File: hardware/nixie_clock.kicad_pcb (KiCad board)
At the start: 2 copper layers, 224 x 70 mm, 66 parts, among them J1 Conn_02x02_Odd_Even, J2 USB_C_Receptacle_USB2.0_16P, J3 Conn_01x03, Q1 IRF740, SW1 SW_SPST, SW2 SW_SPST, U1 AP63203WU, U2 MAX1771xSA, U3 ESP32-C3-WROOM-02, U4 HV5622PG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

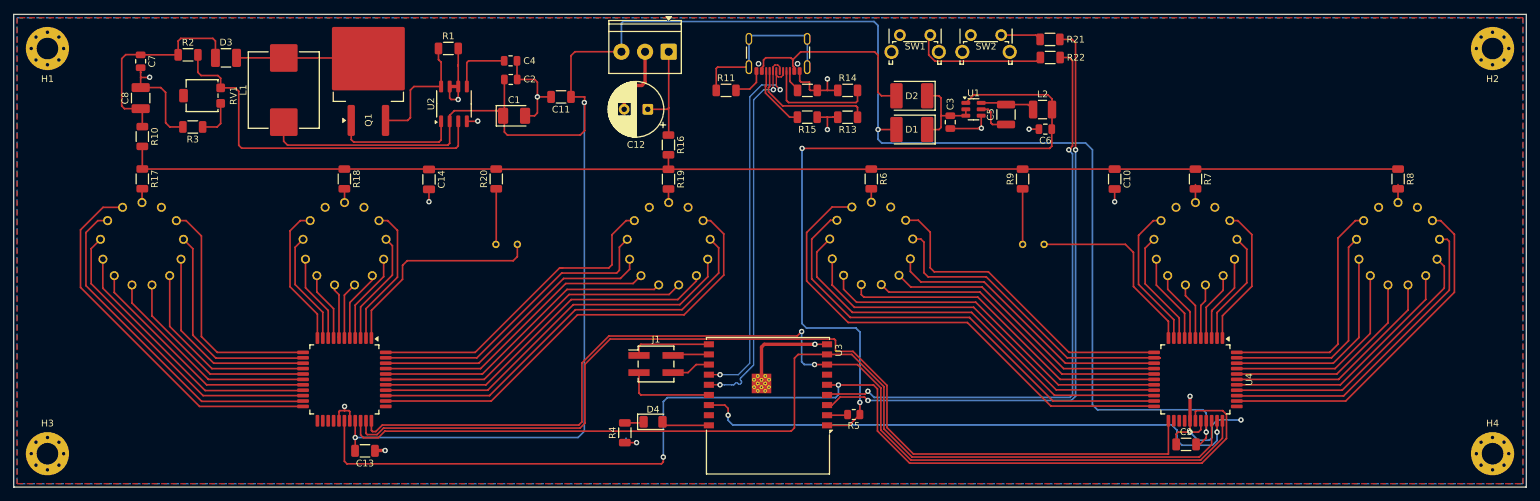
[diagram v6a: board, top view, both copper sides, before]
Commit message: Add decoupling capacitor for MCU. Fix circuit to avoid VCC being between capacitor and power pad.
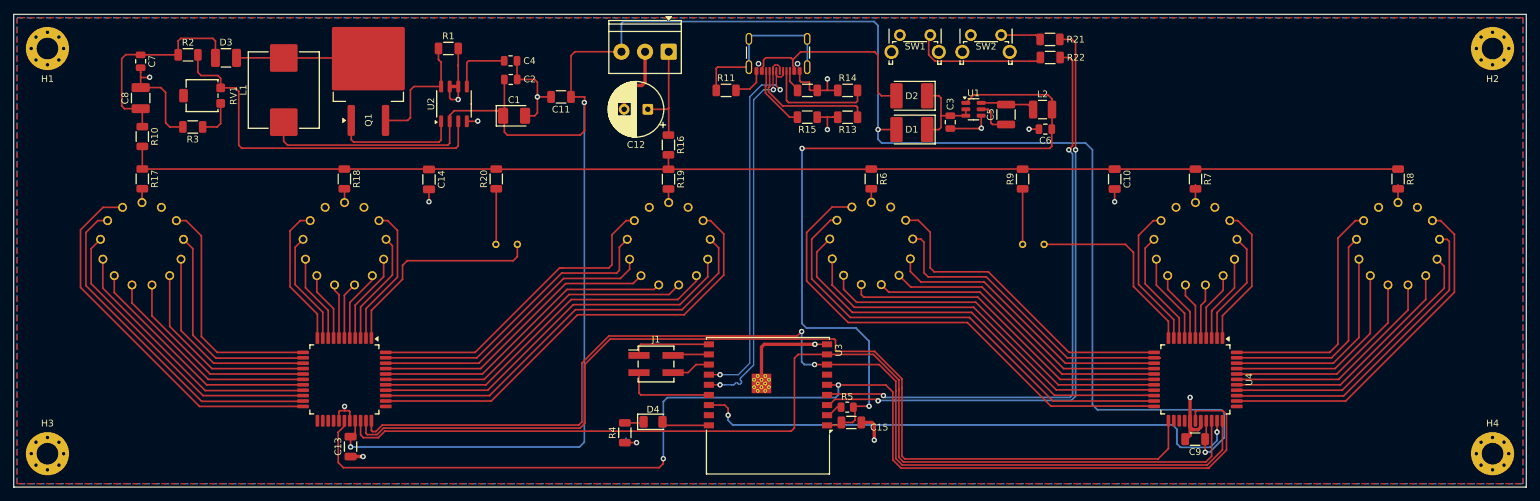
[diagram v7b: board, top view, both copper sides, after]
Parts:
- added C15: 100nF, Capacitor_SMD:C_1206_3216Metric, F.Cu at (174.1, 121.4)
- moved C13 2.22 mm to (99.9, 125.0), turned to 90 degrees
- moved C9 1.54 mm to (224.9, 123.8)
- moved R5 1.46 mm to (173.4, 119.1)
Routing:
- net /connectors/12V: track 327.1 -> 337.0 mm
- net /connectors/GND: track 135.0 -> 126.9 mm, vias 17 -> 16
- net /cpu/SPI_CLK: track 169.1 -> 175.1 mm
- net /cpu/GPIO1: track 156.9 -> 161.5 mm
- net /cpu/GPIO2: track 154.4 -> 159.1 mm
- net /driver_3_digits_1_dot_left/SPI_SDO: track 148.3 -> 151.5 mm
- net /cpu/3.3V: track 110.6 -> 113.5 mm
- net Net-(U3-EN): track 3.26 -> 2.56 mm
- net /cpu/SPI_MOSI: track 82.8 -> 83.5 mm

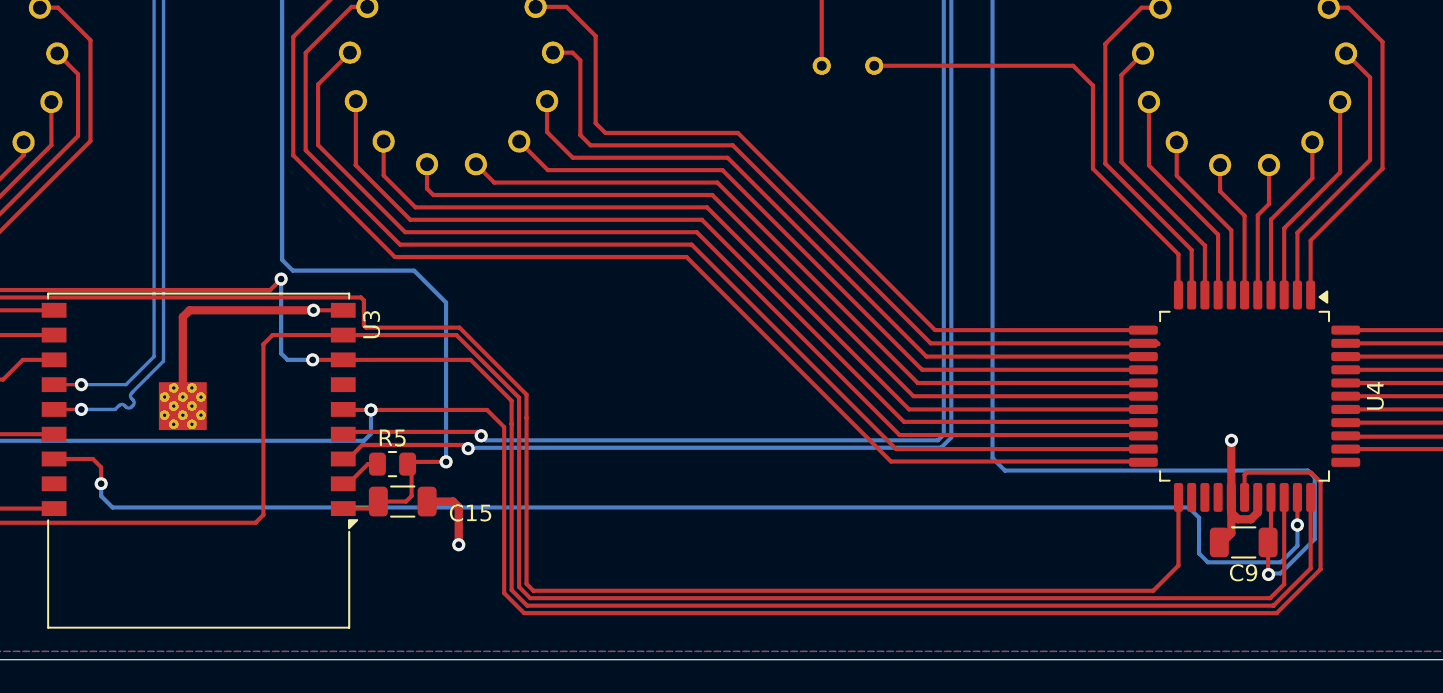
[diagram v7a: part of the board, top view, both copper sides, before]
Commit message: Rework C9. Placed closer to the power pad.
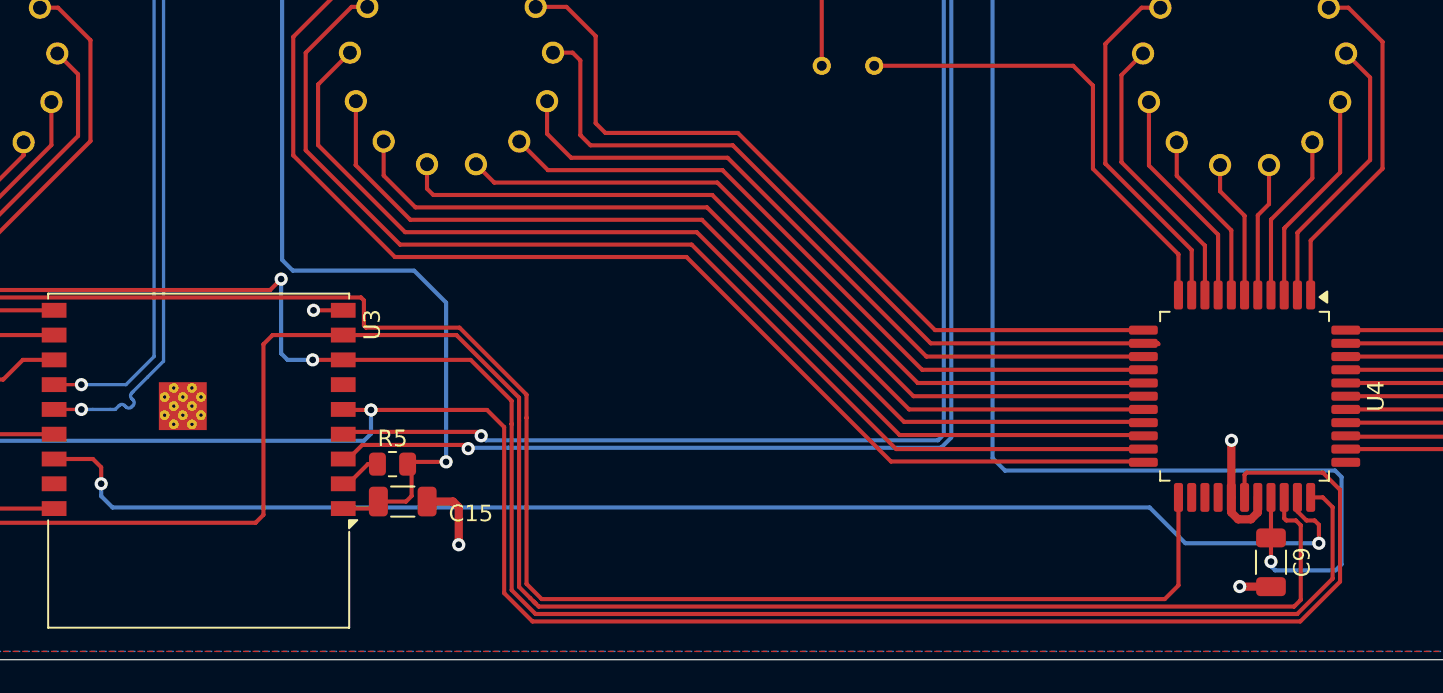
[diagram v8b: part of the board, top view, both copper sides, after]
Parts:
- moved C9 2.04 mm to (226.6, 125.0), turned to 90 degrees
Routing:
- net /connectors/GND: track 126.9 -> 112.1 mm, vias 16 -> 17
- net /connectors/12V: track 337.0 -> 340.1 mm
- net /cpu/GPIO1: track 161.5 -> 164.6 mm
- net /cpu/SPI_CLK: track 175.1 -> 178.1 mm
- net /cpu/GPIO2: track 159.1 -> 162.0 mm
- net /driver_3_digits_1_dot_left/SPI_SDO: track 151.5 -> 152.6 mm
